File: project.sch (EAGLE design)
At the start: 24 parts, among them U1 DSPIC33FJ64MC804-H/PT, U2 TB6612FNG,C,8,EL, U3 FT232RL-REEL, X1 MINI-USB_SHIELD5P2-32005-601, Y1 ABM8-20.000MHZ-B2-T

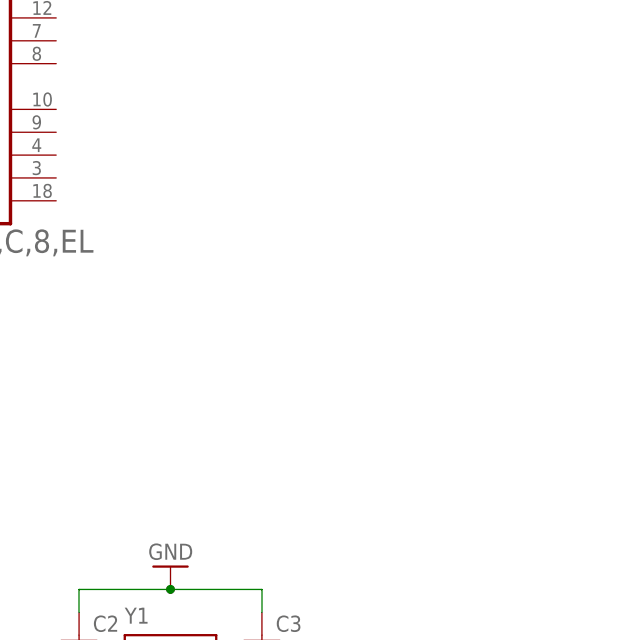
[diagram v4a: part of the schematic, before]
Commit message: Motor Pinout in Schematic
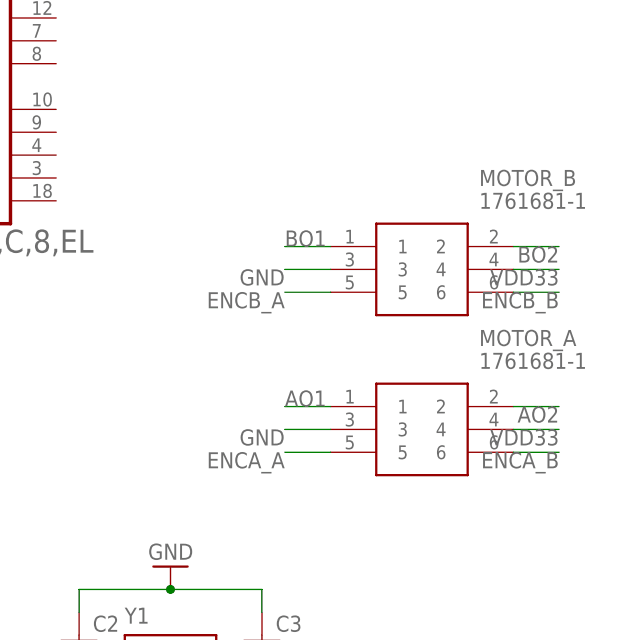
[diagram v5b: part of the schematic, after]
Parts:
- added MOTOR_A, MOTOR_B: 1761681-1, 1761681-1:1761681-1
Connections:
- new net AO1: MOTOR_A.1
- new net AO2: MOTOR_A.2
- new net BO1: MOTOR_B.1
- new net BO2: MOTOR_B.2
- new net ENCA_A: MOTOR_A.5
- new net ENCA_B: MOTOR_A.6
- new net ENCB_A: MOTOR_B.5
- new net ENCB_B: MOTOR_B.6
- new net VDD33: MOTOR_A.4, MOTOR_B.4
- net GND: now also MOTOR_A.3, MOTOR_B.3
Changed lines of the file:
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@@
 <part name="C13" library="capacitor-wima" library_urn="urn:adsk.eagle:library:116" deviceset="C" device="2,5-3" package3d_urn="urn:adsk.eagle:package:5436/1" value="100nF"/>
 <part name="GND18" library="supply1" library_urn="urn:adsk.eagle:library:371" deviceset="GND" device=""/>
+<part name="MOTOR_B" library="1761681-1" deviceset="1761681-1" device=""/>
+<part name="MOTOR_A" library="1761681-1" deviceset="1761681-1" device=""/>
 </parts>
 <sheets>
@@
 <instance part="GND18" gate="1" x="-71.12" y="45.72" smashed="yes">
 <attribute name="VALUE" x="-73.66" y="43.18" size="1.778" layer="96"/>
+</instance>
+<instance part="MOTOR_B" gate="G$1" x="162.56" y="48.26" smashed="yes">
+<attribute name="NAME" x="179.07" y="55.88" size="1.778" layer="95" align="center-left"/>
+<attribute name="VALUE" x="179.07" y="53.34" size="1.778" layer="96" align="center-left"/>
+</instance>
+<instance part="MOTOR_A" gate="G$1" x="162.56" y="30.48" smashed="yes">
+<attribute name="NAME" x="179.07" y="38.1" size="1.778" layer="95" align="center-left"/>
+<attribute name="VALUE" x="179.07" y="35.56" size="1.778" layer="96" align="center-left"/>
 </instance>
 </instances>
@@
 <wire x1="-71.12" y1="53.34" x2="-71.12" y2="48.26" width="0.1524" layer="91"/>
 <pinref part="GND18" gate="1" pin="GND"/>
+</segment>
+<segment>
+<pinref part="MOTOR_B" gate="G$1" pin="3"/>
+<wire x1="162.56" y1="45.72" x2="157.48" y2="45.72" width="0.1524" layer="91"/>
+<label x="157.48" y="45.72" size="1.778" layer="95" rot="R180"/>
+</segment>
+<segment>
+<pinref part="MOTOR_A" gate="G$1" pin="3"/>
+<wire x1="162.56" y1="27.94" x2="157.48" y2="27.94" width="0.1524" layer="91"/>
+<label x="157.48" y="27.94" size="1.778" layer="95" rot="R180"/>
 </segment>
 </net>
@@
 </segment>
 </net>
+<net name="AO2" class="0">
+<segment>
+<pinref part="MOTOR_A" gate="G$1" pin="2"/>
+<wire x1="182.88" y1="30.48" x2="187.96" y2="30.48" width="0.1524" layer="91"/>
+<label x="187.96" y="30.48" size="1.778" layer="95" rot="R180"/>
+</segment>
+</net>
+<net name="VDD33" class="0">
+<segment>
+<pinref part="MOTOR_B" gate="G$1" pin="4"/>
+<wire x1="182.88" y1="45.72" x2="187.96" y2="45.72" width="0.1524" layer="91"/>
+<label x="187.96" y="45.72" size="1.778" layer="95" rot="R180"/>
+</segment>
+<segment>
+<pinref part="MOTOR_A" gate="G$1" pin="4"/>
+<wire x1="182.88" y1="27.94" x2="187.96" y2="27.94" width="0.1524" layer="91"/>
+<label x="187.96" y="27.94" size="1.778" layer="95" rot="R180"/>
+</segment>
+</net>
+<net name="ENCA_B" class="0">
+<segment>
+<pinref part="MOTOR_A" gate="G$1" pin="6"/>
+<wire x1="182.88" y1="25.4" x2="187.96" y2="25.4" width="0.1524" layer="91"/>
+<label x="187.96" y="25.4" size="1.778" layer="95" rot="R180"/>
+</segment>
+</net>
+<net name="ENCA_A" class="0">
+<segment>
+<pinref part="MOTOR_A" gate="G$1" pin="5"/>
+<wire x1="162.56" y1="25.4" x2="157.48" y2="25.4" width="0.1524" layer="91"/>
+<label x="157.48" y="25.4" size="1.778" layer="95" rot="R180"/>
+</segment>
+</net>
+<net name="AO1" class="0">
+<segment>
+<pinref part="MOTOR_A" gate="G$1" pin="1"/>
+<wire x1="162.56" y1="30.48" x2="157.48" y2="30.48" width="0.1524" layer="91"/>
+<label x="157.48" y="30.48" size="1.778" layer="95"/>
+</segment>
+</net>
+<net name="BO2" class="0">
+<segment>
+<pinref part="MOTOR_B" gate="G$1" pin="2"/>
+<wire x1="182.88" y1="48.26" x2="187.96" y2="48.26" width="0.1524" layer="91"/>
+<label x="187.96" y="48.26" size="1.778" layer="95" rot="R180"/>
+</segment>
+</net>
+<net name="ENCB_B" class="0">
+<segment>
+<pinref part="MOTOR_B" gate="G$1" pin="6"/>
+<wire x1="182.88" y1="43.18" x2="187.96" y2="43.18" width="0.1524" layer="91"/>
+<label x="187.96" y="43.18" size="1.778" layer="95" rot="R180"/>
+</segment>
+</net>
+<net name="ENCB_A" class="0">
+<segment>
+<pinref part="MOTOR_B" gate="G$1" pin="5"/>
+<wire x1="162.56" y1="43.18" x2="157.48" y2="43.18" width="0.1524" layer="91"/>
+<label x="157.48" y="43.18" size="1.778" layer="95" rot="R180"/>
+</segment>
+</net>
+<net name="BO1" class="0">
+<segment>
+<pinref part="MOTOR_B" gate="G$1" pin="1"/>
+<wire x1="162.56" y1="48.26" x2="157.48" y2="48.26" width="0.1524" layer="91"/>
+<label x="157.48" y="48.26" size="1.778" layer="95"/>
+</segment>
+</net>

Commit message: add motor, leds, debug pins, replace USBUART with bluetooth ver.
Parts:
- removed C12: 4.7uF, capacitor-wima:C2,5-3
- removed U3: FT232RL-REEL, FT232RL-REEL:FT232RL-REEL
- removed X1: MINI-USB_SHIELD5P2-32005-601, con-cypressindustries:MINI-USB_SHIELD5P2-32005-601
- added BLUETOOTH_UART, JP2: (no value), pinhead:PINHD-1X6
- added C14: 0.33uF, capacitor-wima:C2,5-3
- added C15, C16, C17: 100nF, capacitor-wima:C2,5-3
- added C18: 4.7uF, capacitor-wima:C2,5-3
- added D1: 1N4004, diode:1N4004
- added IC1: UA78M05DCY, linear:UA78M05DCY
- added JP1: (no value), pinhead:PINHD-1X2
- added JP3: (no value), pinhead:PINHD-2X6
- added LED1, LED2, LED3: TLLG4400, led:TLLG4400
- added R4: 47k, rcl:R-EU_0204/2V
- added R5: 4.7k, rcl:R-EU_0204/2V
- added R6, R7, R8: 10k, rcl:R-EU_0204/2V
- added S1, S2: TL32PO, switch:TL32PO
- C10: value 100nF -> 0.1uF
- C11: value 10nF -> 0.1uF
- C13: value 100nF -> 10uF; device capacitor-wima:C2,5-3 -> rcl:CPOL-EU085CS-1AR
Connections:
- removed net 3V3: C13.1, U3.3V3OUT
- removed net DSR: U3.!DSR
- removed net N$4: U3.USBDM, X1G41.4
- removed net N$5: U3.USBDP, X1G41.3
- new net N$10: LED3.A, R8.1
- new net N$11: LED2.A, R7.1
- new net N$12: JP2.4, U1.PGEC1/AN3/C2IN+/RP1/CN5/RB1
- new net N$13: JP2.5, U1.PGED1/AN2/C2IN-/RP0/CN4/RB0
- new net N$14: R5.2, S2.P, U1.INT0/RP7/CN23/PMD5/RB7
- new net N$15: R6.2, U1.PWM2H1/RP22/CN18/PMA1/RC6
- new net N$16: LED1.A, R6.1
- new net N$27: JP3.10
- new net N$28: JP3.12
- new net N$6: C14.1, IC1.VI, JP1.1
- new net N$7: C18.1, U1.VCAP/VDDCORE
- new net N$8: JP2.1, R4.1, S1.S, U1.!MCLR
- new net N$9: D1.A, R4.2
- new net RTS: BLUETOOTH_UART.3, U1.PWM1L2/DAC1RN/RP13/CN13/PMRD/RB13
- net AN0: now also JP3.7
- net AN1: now also JP3.9
- net AN4: now also JP3.11
- net AO1: now also U2.AO1@1, U2.AO1@2
- net AO2: now also U2.AO2@1, U2.AO2@2
- net BO1: now also U2.BO1@1, U2.BO1@2
- net BO2: now also U2.BO2@1, U2.BO2@2
- net CTS: now also BLUETOOTH_UART.6, U1.PWM1H2/DAC1RP/RP12/CN14/PMD0/RB12; no longer U3.!CTS
- net GND: now also BLUETOOTH_UART.2, C13.-, C14.2, C15.2, C16.2, C17.2, C18.2, IC1.GND, IC1.GND@1, JP1.2, JP2.3, LED1.C, LED2.C, LED3.C, R5.1, S1.P, U1.AVSS, U1.VSS, U1.VSS_2, U1.VSS_3, U2.GND; no longer C12.2, C13.2, U3.!RESET, U3.AGND, U3.GND, X1G41.2
- net MTRDRV_AIN1: now also JP3.2, U1.AN8/CVREF/RP18/PMA2/CN10/RC2
- net MTRDRV_AIN2: now also JP3.4, U1.AN7/DAC1LM/RP17/CN9/RC1
- net MTRDRV_BIN1: now also JP3.6, U1.AN6/DAC1RM/RP16/CN8/RC0
- net MTRDRV_BIN2: now also JP3.8, U1.AN5/C1IN+/RP3/CN7/RB3
- net PWMA: now also JP3.1, R8.2, U1.PWM2L1/RP23/CN17/PMA0/RC7
- net PWMB: now also JP3.3, R7.2, U1.PWM1H1/DAC1LP/RTCC/RP14/CN12/PMWR/RB14
- net RX: now also BLUETOOTH_UART.4, U1.PGEC2/PWM1L3/RP11/CN15/PMD1/RB11; no longer U3.TXD
- net STBY: now also JP3.5, U1.SDA1/RP9/CN21/PMD3/RB9
- net TX: now also BLUETOOTH_UART.5, U1.PGED2/EMCD2/PWM1H3/RP10/CN16/PMD2/RB10; no longer U3.RXD
- net VCC: now also C15.1, C16.1, C17.1, D1.C, IC1.VO, JP2.2, S2.S, U1.AVDD, U1.VDD, U1.VDD_2; no longer C10.1, C11.1, C12.1, U3.VCC, X1G41.5
- net VDD33: now also BLUETOOTH_UART.1, C10.1, C11.1, C13.+
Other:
- moved on the sheet: C1, C10, C11, C4, C5, C6, C7, C8, C9, JP1(GP2Y0A51SK0F), JP2(GP2Y0A51SK0F), JP3(GP2Y0A51SK0F)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

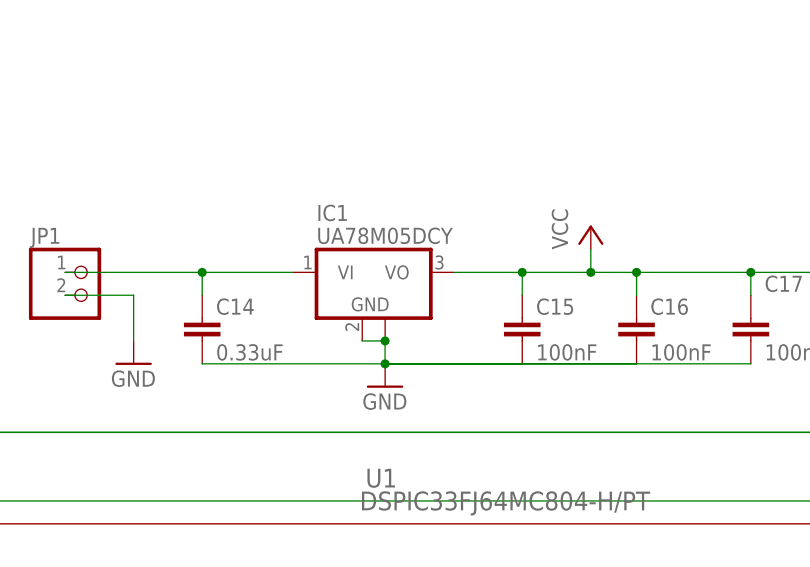
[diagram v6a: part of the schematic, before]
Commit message: Removed Liner Regulator
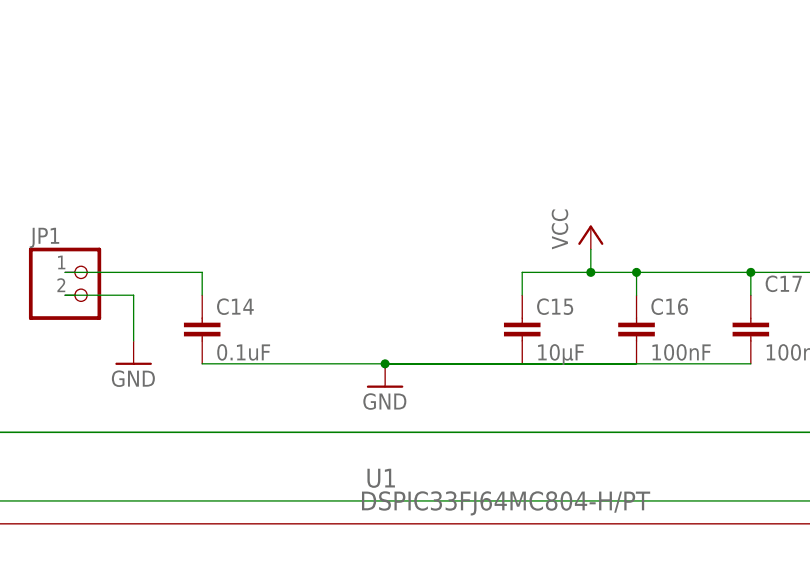
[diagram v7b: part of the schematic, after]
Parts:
- removed IC1: UA78M05DCY, linear:UA78M05DCY
- C14: value 0.33uF -> 0.1uF
- C15: value 100nF -> 10µF
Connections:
- net GND: no longer IC1.GND, IC1.GND@1
- net N$6: no longer IC1.VI
- net VCC: no longer IC1.VO
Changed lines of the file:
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@@
 <part name="C9" library="capacitor-wima" library_urn="urn:adsk.eagle:library:116" deviceset="C" device="2,5-3" package3d_urn="urn:adsk.eagle:package:5436/1" value="10uF"/>
 <part name="GND13" library="supply1" library_urn="urn:adsk.eagle:library:371" deviceset="GND" device=""/>
-<part name="IC1" library="linear" library_urn="urn:adsk.eagle:library:262" deviceset="UA78M*" device="DCY" package3d_urn="urn:adsk.eagle:package:28541/2" technology="05"/>
 <part name="JP1" library="pinhead" library_urn="urn:adsk.eagle:library:325" deviceset="PINHD-1X2" device="" package3d_urn="urn:adsk.eagle:package:22435/2"/>
-<part name="C14" library="capacitor-wima" library_urn="urn:adsk.eagle:library:116" deviceset="C" device="2,5-3" package3d_urn="urn:adsk.eagle:package:5436/1" value="0.33uF"/>
-<part name="C15" library="capacitor-wima" library_urn="urn:adsk.eagle:library:116" deviceset="C" device="2,5-3" package3d_urn="urn:adsk.eagle:package:5436/1" value="100nF"/>
+<part name="C14" library="capacitor-wima" library_urn="urn:adsk.eagle:library:116" deviceset="C" device="2,5-3" package3d_urn="urn:adsk.eagle:package:5436/1" value="0.1uF"/>
+<part name="C15" library="capacitor-wima" library_urn="urn:adsk.eagle:library:116" deviceset="C" device="2,5-3" package3d_urn="urn:adsk.eagle:package:5436/1" value="10µF"/>
 <part name="C16" library="capacitor-wima" library_urn="urn:adsk.eagle:library:116" deviceset="C" device="2,5-3" package3d_urn="urn:adsk.eagle:package:5436/1" value="100nF"/>
 <part name="C17" library="capacitor-wima" library_urn="urn:adsk.eagle:library:116" deviceset="C" device="2,5-3" package3d_urn="urn:adsk.eagle:package:5436/1" value="100nF"/>
@@
 <attribute name="VALUE" x="231.14" y="119.38" size="1.778" layer="96"/>
 </instance>
-<instance part="IC1" gate="G$1" x="25.4" y="58.42" smashed="yes">
-<attribute name="NAME" x="20.32" y="64.135" size="1.778" layer="95"/>
-<attribute name="VALUE" x="20.32" y="61.595" size="1.778" layer="96"/>
-</instance>
 <instance part="JP1" gate="G$1" x="-5.08" y="55.88" smashed="yes">
 <attribute name="NAME" x="-11.43" y="61.595" size="1.778" layer="95"/>
@@
 </segment>
 <segment>
-<pinref part="IC1" gate="G$1" pin="VO"/>
-<wire x1="35.56" y1="58.42" x2="43.18" y2="58.42" width="0.1524" layer="91"/>
 <pinref part="C15" gate="G$1" pin="1"/>
 <wire x1="43.18" y1="58.42" x2="50.8" y2="58.42" width="0.1524" layer="91"/>
@@
 <wire x1="68.58" y1="58.42" x2="78.74" y2="58.42" width="0.1524" layer="91"/>
 <wire x1="43.18" y1="58.42" x2="43.18" y2="55.88" width="0.1524" layer="91"/>
-<junction x="43.18" y="58.42"/>
 <pinref part="C16" gate="G$1" pin="1"/>
 <wire x1="55.88" y1="58.42" x2="55.88" y2="55.88" width="0.1524" layer="91"/>
@@
 </segment>
 <segment>
-<pinref part="IC1" gate="G$1" pin="GND@1"/>
 <pinref part="GND19" gate="1" pin="GND"/>
-<wire x1="27.94" y1="50.8" x2="27.94" y2="48.26" width="0.1524" layer="91"/>
-<pinref part="IC1" gate="G$1" pin="GND"/>
-<wire x1="25.4" y1="50.8" x2="27.94" y2="50.8" width="0.1524" layer="91"/>
-<junction x="27.94" y="50.8"/>
 <pinref part="C14" gate="G$1" pin="2"/>
 <wire x1="7.62" y1="48.26" x2="27.94" y2="48.26" width="0.1524" layer="91"/>
@@
 <segment>
 <pinref part="JP1" gate="G$1" pin="1"/>
-<pinref part="IC1" gate="G$1" pin="VI"/>
 <wire x1="-7.62" y1="58.42" x2="7.62" y2="58.42" width="0.1524" layer="91"/>
 <pinref part="C14" gate="G$1" pin="1"/>
-<wire x1="7.62" y1="58.42" x2="17.78" y2="58.42" width="0.1524" layer="91"/>
 <wire x1="7.62" y1="58.42" x2="7.62" y2="55.88" width="0.1524" layer="91"/>
-<junction x="7.62" y="58.42"/>
-</segment>
-</net>
+</segment>
+</net>
